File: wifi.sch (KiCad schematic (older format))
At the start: 5 parts, among them J3 WIFI_OFF, U9 ESP32-WROOM

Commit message: schematics: documented ESP32 pinout from old versions
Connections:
- net labels added: GN13
- net labels removed: GN10
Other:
- note added: "GN11 <v3.1 GP11 <v2.0.6"
- note added: "GN12 <v3.1 GP12 <v2.0.6"
- note added: "GP11 <v3.1 GN11 <v2.0.6"
- note added: "GP12 <v3.1 GN12 <v2.0.6"
- note added: "GP13 <v3.1 GN13 <v2.0.6"
- note added: "NC <v3.1 GP10 v1.7"
- note removed: "GN11 <v2.0.6"
- note removed: "GN12 <v2.0.6"
- note removed: "GN13 <v2.0.6"
- note removed: "GP10 v1.7, NC <v3.1"
- note removed: "GP11 <v2.0.6"
- note removed: "GP12 <v2.0.6"
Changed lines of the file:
@@
 Text Notes 9250 4650 0    60   ~ 0
 Strapping pins\n(avoid using to avoid\nboot problems)\nGPIO0,2,4,5,12,15
-Text Notes 2750 5350 0    60   ~ 0
+Text Notes 2500 6500 0    60   ~ 0
 ESP32 ADC capable pins\nGPIO36,39,34,35,32,33,25,26,27,\nGPIO14,12,13,15 - shared with HSPI/JTAG\nConnected to BANK7 on "gpio" sheet
-Text Notes 3650 6000 0    60   ~ 0
+Text Notes 3400 7150 0    60   ~ 0
 ESP32 HSPI pins\nGPIO12: MISO\nGPIO13: MOSI\nGPIO14: SCK\nGPIO15: SS
-Text Notes 4550 6300 0    60   ~ 0
+Text Notes 4300 7450 0    60   ~ 0
 ESP32 JTAG slave interface\nEN: TRST_N\nGPIO15: TDO\nGPIO12: TDI\nGPIO13: TCK\nGPIO14: TMS\nFLASH over JTAG\nnot yet supported.
-Text Notes 2750 6000 0    60   ~ 0
+Text Notes 2500 7150 0    60   ~ 0
 ESP32 VSPI pins\nGPIO5: SS\nGPIO18: SCK\nGPIO19: MISO\nGPIO23: MOSI
-Text GLabel 5700 3350 0    60   Input ~ 0
+Text GLabel 5700 3450 0    60   Input ~ 0
 GP13
+Text GLabel 5700 3650 0    60   Input ~ 0
+GP12
 Text GLabel 5700 3550 0    60   Input ~ 0
-GP12
-Text GLabel 5700 3450 0    60   Input ~ 0
 GN12
+Text GLabel 5700 3850 0    60   Input ~ 0
+GP11
 Text GLabel 5700 3750 0    60   Input ~ 0
-GP11
-Text GLabel 5700 3650 0    60   Input ~ 0
 GN11
 Text GLabel 7550 3900 2    60   Input ~ 0
@@
 WIFIEN
 Connection ~ 4550 2950
-Text Notes 1350 4500 0    60   ~ 0
+Text Notes 1350 5300 0    60   ~ 0
 GPIO12 probably should be held low at reset or disconnected\nother option is to burn flash voltage efuse for 3.3V operation\nfor GPIO2 and GPIO12 bootstrapping considerations, read\nhttps://github.com/espressif/esp-idf/tree/master/examples/storage/sd_card
+Text Notes 1350 5600 0    60   ~ 0
+GPIO25,26 are DAC channels that can directly replay\naudio material over i2s bus
 Text Notes 1350 4800 0    60   ~ 0
-GPIO25,26 are DAC channels that can directly replay\naudio material over i2s bus
-Text Notes 1350 4000 0    60   ~ 0
 SD card connected according to\nArduino->Examples->ESP32->SD_MMC_Test\nhttps://github.com/espressif/esp-idf/blob/\nmaster/examples/storage/sd_card/README.md\n
-Text Notes 4500 4000 0    60   ~ 0
+Text Notes 3150 4000 0    60   ~ 0
 GN10 v1.7
-Text Notes 4550 4100 0    60   ~ 0
+Text Notes 3150 4100 0    60   ~ 0
 GP9 v1.7
 Text Notes 6350 5750 1    60   ~ 0
@@
 Text Notes 7350 5700 0    60   ~ 0
 LED and WIFI_GPIO17\nto solder pads of PCB
-Text Notes 4350 3900 0    60   ~ 0
-GP10 v1.7, NC <v3.1
+Text Notes 3150 3900 0    60   ~ 0
+NC <v3.1 GP10 v1.7
 NoConn ~ 5700 3150
 NoConn ~ 5700 3050
@@
 Wire Wire Line
 	4550 2950 4550 3000
-Text Notes 4750 3800 0    60   ~ 0
-GN11 <v2.0.6
-Text Notes 4750 3700 0    60   ~ 0
-GP11 <v2.0.6
-Text Notes 4750 3600 0    60   ~ 0
-GN12 <v2.0.6
-Text Notes 4750 3500 0    60   ~ 0
-GP12 <v2.0.6
-Text Notes 4750 3400 0    60   ~ 0
-GN13 <v2.0.6
+Text Notes 3150 3800 0    60   ~ 0
+GP11 <v3.1 GN11 <v2.0.6
+Text Notes 3150 3700 0    60   ~ 0
+GN11 <v3.1 GP11 <v2.0.6
+Text Notes 3150 3600 0    60   ~ 0
+GP12 <v3.1 GN12 <v2.0.6
+Text Notes 3150 3500 0    60   ~ 0
+GN12 <v3.1 GP12 <v2.0.6
+Text Notes 3150 3400 0    60   ~ 0
+GP13 <v3.1 GN13 <v2.0.6
 Text Notes 3750 3300 0    60   ~ 0
 GP13 <v2.0.6
@@
 Text Notes 3150 3300 0    60   ~ 0
 GN13 <v3.1
-Text GLabel 5700 3850 0    60   Input ~ 0
-GN10
 Text GLabel 7550 3300 2    60   Input ~ 0
 WIFI_GPIO21
+Text GLabel 5700 3350 0    60   Input ~ 0
+GN13
 $EndSCHEMATC

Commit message: schematics: wifi updated pinout GP13 separated
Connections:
- net labels added: GN10, GP10
- no-connect marks 8 -> 6
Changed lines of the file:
@@
 Text Notes 2500 7150 0    60   ~ 0
 ESP32 VSPI pins\nGPIO5: SS\nGPIO18: SCK\nGPIO19: MISO\nGPIO23: MOSI
+Text GLabel 5700 3050 0    60   Input ~ 0
+GP13
+Text GLabel 5700 3550 0    60   Input ~ 0
+GP12
 Text GLabel 5700 3450 0    60   Input ~ 0
-GP13
+GN12
+Text GLabel 5700 3750 0    60   Input ~ 0
+GP11
 Text GLabel 5700 3650 0    60   Input ~ 0
-GP12
-Text GLabel 5700 3550 0    60   Input ~ 0
-GN12
-Text GLabel 5700 3850 0    60   Input ~ 0
-GP11
-Text GLabel 5700 3750 0    60   Input ~ 0
 GN11
 Text GLabel 7550 3900 2    60   Input ~ 0
@@
 Text Notes 3150 3900 0    60   ~ 0
 NC <v3.1 GP10 v1.7
-NoConn ~ 5700 3150
-NoConn ~ 5700 3050
 Wire Wire Line
 	4550 2550 4550 2600
@@
 Text GLabel 7550 3300 2    60   Input ~ 0
 WIFI_GPIO21
+Text GLabel 5700 3150 0    60   Input ~ 0
+GN13
+Text GLabel 5700 3850 0    60   Input ~ 0
+GP10
 Text GLabel 5700 3350 0    60   Input ~ 0
-GN13
+GN10
 $EndSCHEMATC

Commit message: schematics: some PN's for LCSC
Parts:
- U9: LCSC (none) -> C529581
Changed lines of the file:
@@
 F 8 "3.32€" H 6650 3450 50  0001 C CNN "price100_Mouser"
 F 9 "1904-1010-1-ND" H 6650 3450 50  0001 C CNN "Digikey"
-F 10 "Leave empty" H 6650 3450 50  0001 C CNN "LowCost"
-F 11 "FU001" H 6650 3450 50  0001 C CNN "Koncar"
+F 10 "C529581" H 6650 3450 50  0001 C CNN "LCSC"
+F 11 "Leave empty" H 6650 3450 50  0001 C CNN "LowCost"
+F 12 "FU001" H 6650 3450 50  0001 C CNN "Koncar"
 	1    6650 3450
 	1    0    0    -1

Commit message: schematics: preparation for v3.1.2 WROOM/WROVER compatibility
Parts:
- U9: value ESP32-WROOM -> ESP32
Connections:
- net labels removed: WIFI_GPIO16, WIFI_GPIO17
- no-connect marks 6 -> 8
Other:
- note added: "NC >=v3.1.2"
- note added: "NC v1.7, >=v3.1.2"
- note added: "WROVER GPIO16,17\nused internally for PSRAM"
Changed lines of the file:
@@
 Title "ULX3S"
 Date ""
-Rev "1.0.3"
+Rev "1.0.4"
 Comp "EMARD"
 Comment1 "WIFI module ESP32"
@@
 P 6650 3450
 F 0 "U9" H 5950 4700 60  0000 C CNN
-F 1 "ESP32-WROOM" H 6950 4700 60  0000 C CNN
+F 1 "ESP32" H 7200 4700 60  0000 C CNN
 F 2 "ESP32:ESP32-WROOM32" H 7000 4800 60  0001 C CNN
 F 3 "http://espressif.com/sites/default/files/documentation/esp32_datasheet_en.pdf" H 6200 3900 60  0001 C CNN
@@
 Text GLabel 5700 3650 0    60   Input ~ 0
 GN11
-Text GLabel 7550 3900 2    60   Input ~ 0
-WIFI_GPIO16
 $Comp
 L power:GND #PWR0123
@@
 Wire Wire Line
 	4550 2900 4550 2950
-Text GLabel 7550 3800 2    60   Input ~ 0
-WIFI_GPIO17
 Wire Wire Line
 	4550 2950 5700 2950
@@
 NC v1.7, WIFI_GPIO5 <v3.1
 Text Notes 8550 3850 0    60   ~ 0
-NC v1.7
+NC v1.7, >=v3.1.2
 Text Notes 8550 4050 0    60   ~ 0
 NC v1.7
@@
 Text GLabel 5700 3350 0    60   Input ~ 0
 GN10
+Text Notes 8550 3950 0    60   ~ 0
+NC >=v3.1.2
+NoConn ~ 7550 3800
+NoConn ~ 7550 3900
+Text Notes 9550 3950 0    60   ~ 0
+WROVER GPIO16,17\nused internally for PSRAM
 $EndSCHEMATC

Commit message: schematics: update esp32 symbol
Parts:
- U9: footprint ESP32:ESP32-WROOM32 -> ESP32:ESP32; symbol esp-wroom32:ESP-WROOM32 -> esp32:ESP32-WROOM-WROVER
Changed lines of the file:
@@
 Text GLabel 7100 4500 3    60   Input ~ 0
 SD_D0
-Text GLabel 7550 4000 2    60   Input ~ 0
+Text GLabel 7550 3950 2    60   Input ~ 0
 SD_D1
 Text GLabel 6300 4500 3    60   Input ~ 0
@@
 Text GLabel 5700 4050 0    60   Input ~ 0
 SD_D2
-Text GLabel 7550 3200 2    60   Input ~ 0
+Text GLabel 7550 3150 2    60   Input ~ 0
 WIFI_RXD
-Text GLabel 7550 3100 2    60   Input ~ 0
+Text GLabel 7550 3050 2    60   Input ~ 0
 WIFI_TXD
-Text GLabel 7550 4100 2    60   Input ~ 0
+Text GLabel 7550 4050 2    60   Input ~ 0
 WIFI_GPIO0
-Text GLabel 7550 2900 2    60   Input ~ 0
+Text GLabel 7550 2850 2    60   Input ~ 0
 JTAG_TDI
 Text GLabel 5700 3250 0    60   Input ~ 0
 JTAG_TDO
-Text GLabel 7550 3600 2    60   Input ~ 0
+Text GLabel 7550 3550 2    60   Input ~ 0
 JTAG_TCK
-Text GLabel 7550 3700 2    60   Input ~ 0
+Text GLabel 7550 3650 2    60   Input ~ 0
 JTAG_TMS
 $Comp
-L esp-wroom32:ESP-WROOM32 U9
+L esp32:ESP32-WROOM-WROVER U9
 U 1 1 58E5662B
 P 6650 3450
+AR Path="/58E5662B" Ref="U9"  Part="1"
+AR Path="/58D6D447/58E5662B" Ref="U9"  Part="1"
 F 0 "U9" H 5950 4700 60  0000 C CNN
 F 1 "ESP32" H 7200 4700 60  0000 C CNN
-F 2 "ESP32:ESP32-WROOM32" H 7000 4800 60  0001 C CNN
+F 2 "ESP32:ESP32" H 7000 4800 60  0001 C CNN
 F 3 "http://espressif.com/sites/default/files/documentation/esp32_datasheet_en.pdf" H 6200 3900 60  0001 C CNN
 F 4 "espressif.com" H 6650 3450 60  0001 C CNN "MNF1_URL"
@@
 L power:GND #PWR0123
 U 1 1 59C1BF96
-P 7650 2800
-F 0 "#PWR0123" H 7650 2550 50  0001 C CNN
-F 1 "GND" H 7650 2650 50  0000 C CNN
-F 2 "" H 7650 2800 50  0001 C CNN
-F 3 "" H 7650 2800 50  0001 C CNN
-	1    7650 2800
+P 7650 2750
+F 0 "#PWR0123" H 7650 2500 50  0001 C CNN
+F 1 "GND" H 7650 2600 50  0000 C CNN
+F 2 "" H 7650 2750 50  0001 C CNN
+F 3 "" H 7650 2750 50  0001 C CNN
+	1    7650 2750
 	0    -1   -1   0
 $EndComp
 Wire Wire Line
-	7550 2800 7650 2800
+	7550 2750 7650 2750
 $Comp
 L power:GND #PWR0122
 U 1 1 59C1BFCC
-P 7650 2700
-F 0 "#PWR0122" H 7650 2450 50  0001 C CNN
-F 1 "GND" H 7650 2550 50  0000 C CNN
-F 2 "" H 7650 2700 50  0001 C CNN
-F 3 "" H 7650 2700 50  0001 C CNN
-	1    7650 2700
+P 7650 2650
+F 0 "#PWR0122" H 7650 2400 50  0001 C CNN
+F 1 "GND" H 7650 2500 50  0000 C CNN
+F 2 "" H 7650 2650 50  0001 C CNN
+F 3 "" H 7650 2650 50  0001 C CNN
+	1    7650 2650
 	0    -1   -1   0
 $EndComp
 Wire Wire Line
-	7550 2700 7650 2700
-Text GLabel 7550 3000 2    60   Input ~ 0
+	7550 2650 7650 2650
+Text GLabel 7550 2950 2    60   Input ~ 0
 WIFI_GPIO22
 $Comp
@@
 Text Notes 7150 6200 1    60   ~ 0
 WIFI_LED v1.7
-Text GLabel 7550 3500 2    60   Input ~ 0
+Text GLabel 7550 3450 2    60   Input ~ 0
 WIFI_GPIO19
 Text Notes 8550 3750 0    60   ~ 0
@@
 Text Notes 3150 3300 0    60   ~ 0
 GN13 <v3.1
-Text GLabel 7550 3300 2    60   Input ~ 0
+Text GLabel 7550 3250 2    60   Input ~ 0
 WIFI_GPIO21
 Text GLabel 5700 3150 0    60   Input ~ 0
@@
 Text Notes 8550 3950 0    60   ~ 0
 NC >=v3.1.2
-NoConn ~ 7550 3800
-NoConn ~ 7550 3900
+NoConn ~ 7550 3750
+NoConn ~ 7550 3850
 Text Notes 9550 3950 0    60   ~ 0
 WROVER GPIO16,17\nused internally for PSRAM

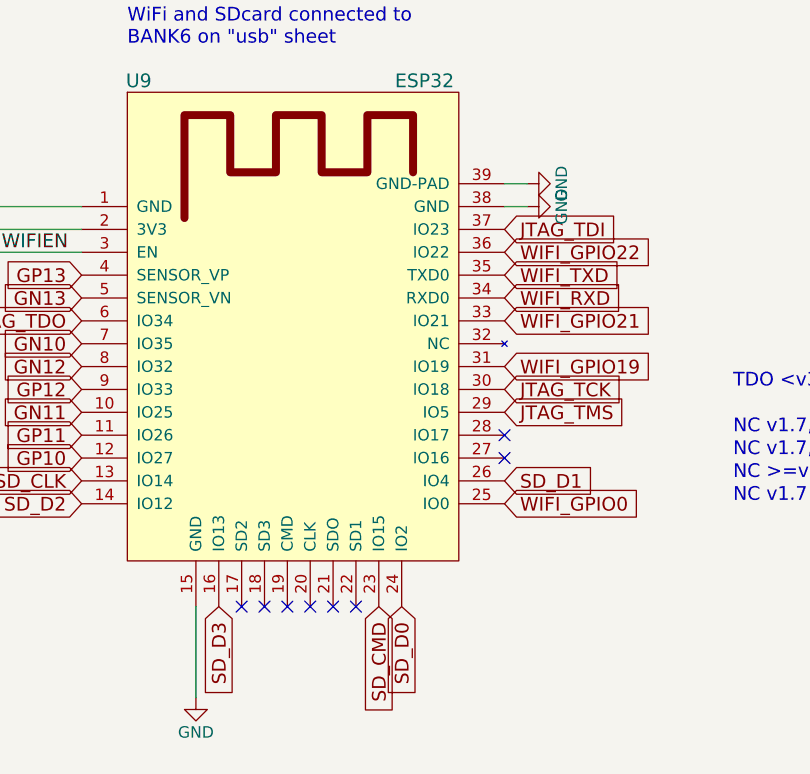
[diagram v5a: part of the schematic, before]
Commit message: schematics: wifi page updated (remove unconnected pins)
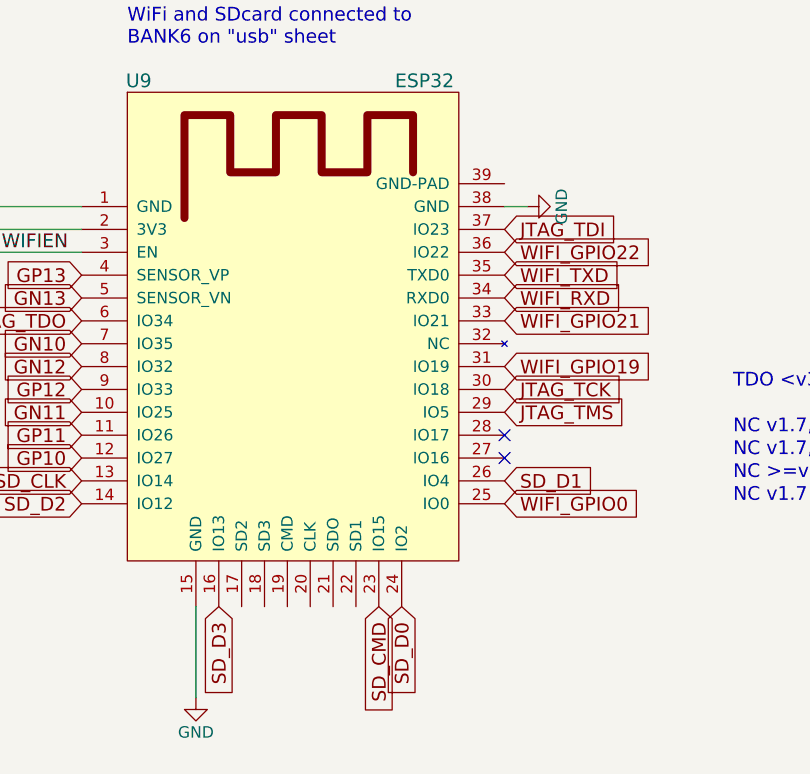
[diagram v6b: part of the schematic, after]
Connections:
- net GND: no longer U9.39 (GND-PAD)
- no-connect marks 8 -> 2
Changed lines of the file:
@@
 Title "ULX3S"
 Date ""
-Rev "1.0.4"
+Rev "1.0.5"
 Comp "EMARD"
 Comment1 "WIFI module ESP32"
@@
 Wire Wire Line
 	7550 2750 7650 2750
-$Comp
-L power:GND #PWR0122
-U 1 1 59C1BFCC
-P 7650 2650
-F 0 "#PWR0122" H 7650 2400 50  0001 C CNN
-F 1 "GND" H 7650 2500 50  0000 C CNN
-F 2 "" H 7650 2650 50  0001 C CNN
-F 3 "" H 7650 2650 50  0001 C CNN
-	1    7650 2650
-	0    -1   -1   0
-$EndComp
-Wire Wire Line
-	7550 2650 7650 2650
 Text GLabel 7550 2950 2    60   Input ~ 0
 WIFI_GPIO22
@@
 Text Notes 3750 3300 0    60   ~ 0
 GP13 <v2.0.6
-NoConn ~ 6400 4500
-NoConn ~ 6500 4500
-NoConn ~ 6600 4500
-NoConn ~ 6700 4500
-NoConn ~ 6800 4500
-NoConn ~ 6900 4500
 Text Notes 8550 3550 0    60   ~ 0
 TDO <v3.1

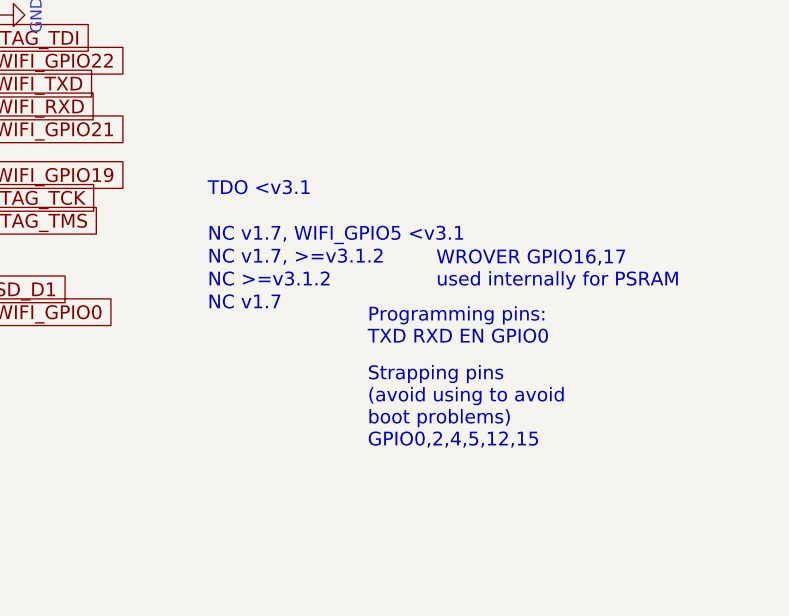
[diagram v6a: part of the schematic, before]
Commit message: schematics: wifi page updated texutal comment align with pins
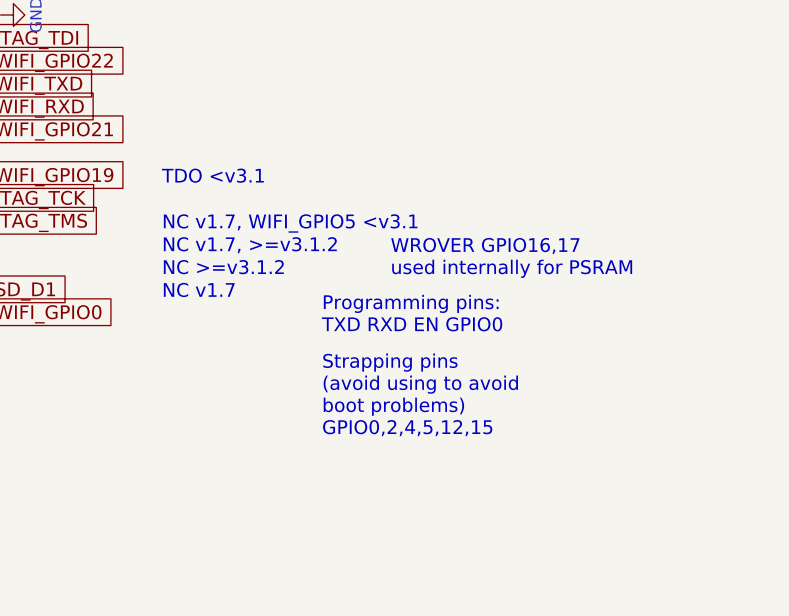
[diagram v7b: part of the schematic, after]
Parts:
- U9: MPN ESP-WROOM-32 -> ESP32-WROVER-E; Mouse_r1 (none) -> 356-ESPWROOM3216MB; Mouser 356-ESPWROOM3216MB -> 356-ESP32WRVE22864PC
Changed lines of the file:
@@
 Title "ULX3S"
 Date ""
-Rev "1.0.5"
+Rev "1.0.6"
 Comp "EMARD"
 Comment1 "WIFI module ESP32"
@@
 F 1 "ESP32" H 7200 4700 60  0000 C CNN
 F 2 "ESP32:ESP32" H 7000 4800 60  0001 C CNN
-F 3 "http://espressif.com/sites/default/files/documentation/esp32_datasheet_en.pdf" H 6200 3900 60  0001 C CNN
+F 3 "https://www.espressif.com/sites/default/files/documentation/esp32-wrover-e_esp32-wrover-ie_datasheet_en.pdf" H 6200 3900 60  0001 C CNN
 F 4 "espressif.com" H 6650 3450 60  0001 C CNN "MNF1_URL"
-F 5 "ESP-WROOM-32" H 6650 3450 60  0001 C CNN "MPN"
-F 6 "356-ESPWROOM3216MB" H 6650 3450 50  0001 C CNN "Mouser"
-F 7 "356-ESP-WROOM-32 " H 6650 3450 50  0001 C CNN "Mouse_r2"
-F 8 "3.32€" H 6650 3450 50  0001 C CNN "price100_Mouser"
-F 9 "1904-1010-1-ND" H 6650 3450 50  0001 C CNN "Digikey"
-F 10 "C529581" H 6650 3450 50  0001 C CNN "LCSC"
-F 11 "Leave empty" H 6650 3450 50  0001 C CNN "LowCost"
-F 12 "FU001" H 6650 3450 50  0001 C CNN "Koncar"
+F 5 "ESP32-WROVER-E" H 6650 3450 60  0001 C CNN "MPN"
+F 6 "356-ESP32WRVE22864PC" H 6650 3450 50  0001 C CNN "Mouser"
+F 7 "356-ESPWROOM3216MB" H 6650 3450 50  0001 C CNN "Mouse_r1"
+F 8 "356-ESP-WROOM-32 " H 6650 3450 50  0001 C CNN "Mouse_r2"
+F 9 "3.32€" H 6650 3450 50  0001 C CNN "price100_Mouser"
+F 10 "1904-1010-1-ND" H 6650 3450 50  0001 C CNN "Digikey"
+F 11 "C529581" H 6650 3450 50  0001 C CNN "LCSC"
+F 12 "Leave empty" H 6650 3450 50  0001 C CNN "LowCost"
+F 13 "FU001" H 6650 3450 50  0001 C CNN "Koncar"
 	1    6650 3450
 	1    0    0    -1
@@
 	0    -1   -1   0
 $EndComp
-Text Notes 9250 4200 0    60   ~ 0
+Text Notes 9050 4150 0    60   ~ 0
 Programming pins:\nTXD RXD EN GPIO0
 $Comp
@@
 Text Notes 5900 2050 0    60   ~ 0
 WiFi and SDcard connected to\nBANK6 on "usb" sheet
-Text Notes 9250 4650 0    60   ~ 0
+Text Notes 9050 4600 0    60   ~ 0
 Strapping pins\n(avoid using to avoid\nboot problems)\nGPIO0,2,4,5,12,15
 Text Notes 2500 6500 0    60   ~ 0
@@
 Text GLabel 7550 3450 2    60   Input ~ 0
 WIFI_GPIO19
-Text Notes 8550 3750 0    60   ~ 0
+Text Notes 8350 3700 0    60   ~ 0
 NC v1.7, WIFI_GPIO5 <v3.1
-Text Notes 8550 3850 0    60   ~ 0
+Text Notes 8350 3800 0    60   ~ 0
 NC v1.7, >=v3.1.2
-Text Notes 8550 4050 0    60   ~ 0
+Text Notes 8350 4000 0    60   ~ 0
 NC v1.7
 Text Notes 7350 5700 0    60   ~ 0
@@
 Text Notes 3750 3300 0    60   ~ 0
 GP13 <v2.0.6
-Text Notes 8550 3550 0    60   ~ 0
+Text Notes 8350 3500 0    60   ~ 0
 TDO <v3.1
 Text Notes 3150 3300 0    60   ~ 0
@@
 Text GLabel 5700 3350 0    60   Input ~ 0
 GN10
-Text Notes 8550 3950 0    60   ~ 0
+Text Notes 8350 3900 0    60   ~ 0
 NC >=v3.1.2
 NoConn ~ 7550 3750
 NoConn ~ 7550 3850
-Text Notes 9550 3950 0    60   ~ 0
+Text Notes 9350 3900 0    60   ~ 0
 WROVER GPIO16,17\nused internally for PSRAM
 $EndSCHEMATC

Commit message: schematics: wifi PN for WROVER-E Digikey, LCSC
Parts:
- U9: Digike_y2 (none) -> 1904-1010-1-ND; Digikey 1904-1010-1-ND -> 1965-ESP32-WROVER-B(16MB)CT-ND; LCSC C529581 -> C529589; LCS_C2 (none) -> C529581
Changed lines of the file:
@@
 F 8 "356-ESP-WROOM-32 " H 6650 3450 50  0001 C CNN "Mouse_r2"
 F 9 "3.32€" H 6650 3450 50  0001 C CNN "price100_Mouser"
-F 10 "1904-1010-1-ND" H 6650 3450 50  0001 C CNN "Digikey"
-F 11 "C529581" H 6650 3450 50  0001 C CNN "LCSC"
-F 12 "Leave empty" H 6650 3450 50  0001 C CNN "LowCost"
-F 13 "FU001" H 6650 3450 50  0001 C CNN "Koncar"
+F 10 "1965-ESP32-WROVER-B(16MB)CT-ND" H 6650 3450 50  0001 C CNN "Digikey"
+F 11 "1904-1010-1-ND" H 6650 3450 50  0001 C CNN "Digike_y2"
+F 12 "C529589" H 6650 3450 50  0001 C CNN "LCSC"
+F 13 "C529581" H 6650 3450 50  0001 C CNN "LCS_C2"
+F 14 "Leave empty" H 6650 3450 50  0001 C CNN "LowCost"
+F 15 "FU001" H 6650 3450 50  0001 C CNN "Koncar"
 	1    6650 3450
 	1    0    0    -1
